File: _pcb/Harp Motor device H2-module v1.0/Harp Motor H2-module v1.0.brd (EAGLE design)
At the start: 58 x 52.5 mm, 80 parts, among them IC1 FT232RL, IC10 OPA365, IC11 74LVC1G125DBV, IC12 74LVC1G125DBV, IC3 LP5907MFX-3.3, IC7 USBLC6-2SC6, IC8 ATXMEGA32A4U, IC9 TLV70033DDCR, T1 DMG1012UW??, T2 DMG1012UW??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

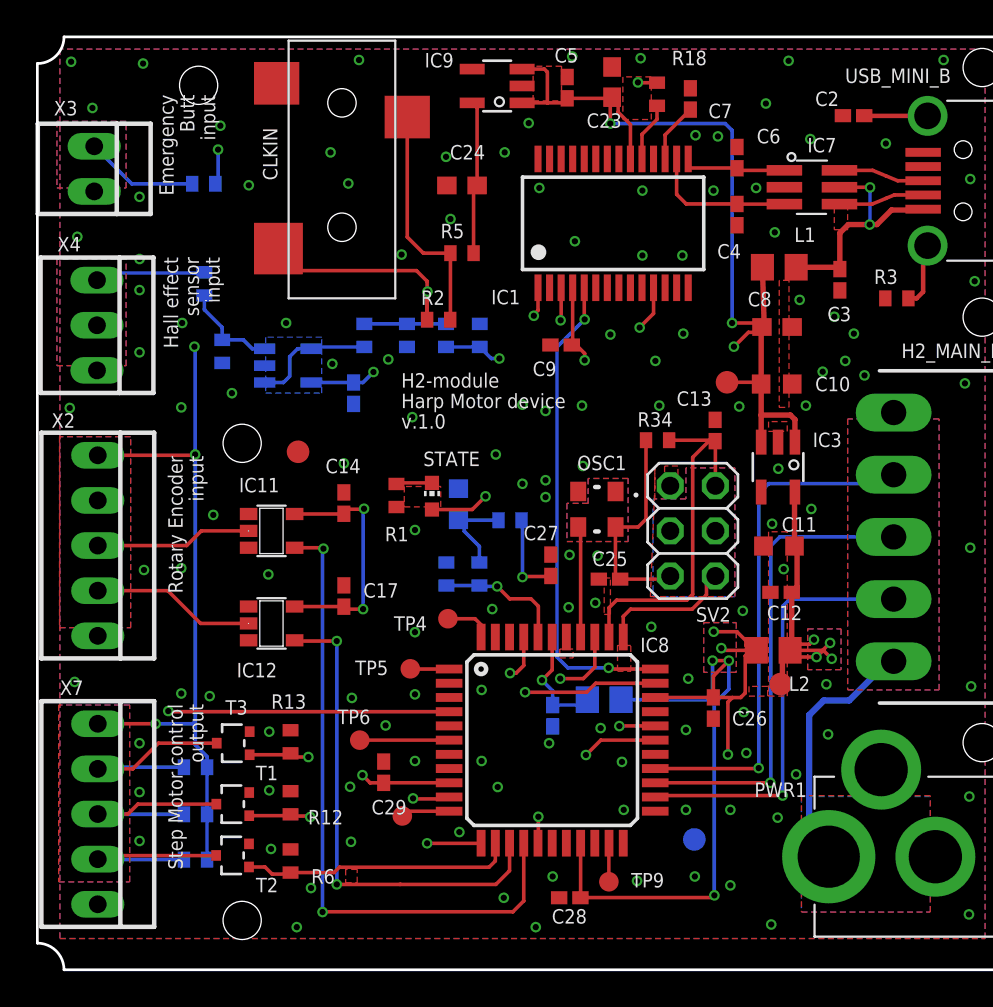
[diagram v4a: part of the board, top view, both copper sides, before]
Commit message: Harp Motor device H2-module v1.0 - last revision with Filipe
- extra R0 on some stages
- IO headers - GND pin was on wrong end
- rebuild user-friend labelling

- still missing OEPS components code & BOM
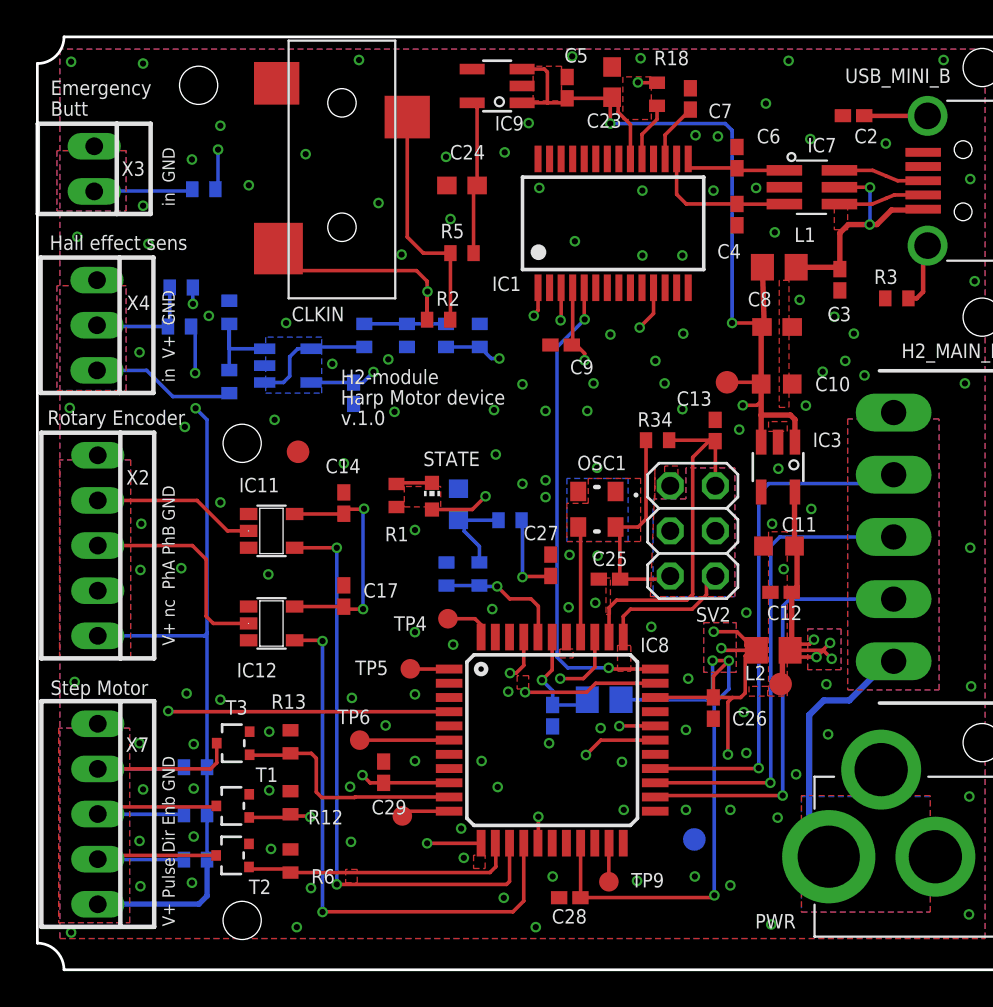
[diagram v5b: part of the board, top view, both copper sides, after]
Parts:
- added R10: DNI, Harp Motor H2-module v1.0:R0402$1
- added R11: 0R, Harp Motor H2-module v1.0:R0402$1
- moved R20 5.68 mm to (10.8, 33.1), turned to 270 degrees
- moved R21 2.24 mm to (10.8, 37.0), turned to 270 degrees
- moved R8 0.30 mm to (9.37, 43.9)
- moved T1 0.10 mm to (11.0, 9.22)
- renumbered PWR1 to PWR
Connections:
- new net N$51: R10.1, R11.1, X4.2
- net +3V3: now also R11.2; no longer X4.2
- net +5V: now also R10.2, X2.5, X7.5; no longer X2.1, X7.1
- net EMERGENCY_INPUT: now also X3.2; no longer X3.1
- net ENCODER_A_PHASE: now also IC12.2; no longer IC11.2
- net ENCODER_B_PHASE: now also IC11.2, X2.2; no longer IC12.2, X2.4
- net GND: now also X2.1, X3.1, X4.1, X7.1; no longer X2.5, X3.2, X4.3, X7.5
- net HALL_EFFCT_IN: now also X4.3; no longer X4.1
- net STEP_ENABLE: now also R14.1, T3.3, X7.2; no longer R16.1, T2.3, X7.4
- net STEP_PULSE: now also R16.1, T2.3, X7.4; no longer R14.1, T3.3, X7.2
- net U_ENCODER_A_PHASE: now also IC12.4; no longer IC11.4
- net U_ENCODER_B_PHASE: now also IC11.4; no longer IC12.4
- net U_STEP_ENABLE: now also IC8.10, R13.2, T3.1; no longer IC8.13, R6.2, T2.1
- net U_STEP_PULSE: now also IC8.13, R6.2, T2.1; no longer IC8.10, R13.2, T3.1
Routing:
- net N$51: track 0.00 -> 6.27 mm
- net U_ENCODER_B_PHASE: track 27.7 -> 33.3 mm
- net +5V: track 121.3 -> 126.7 mm, vias 6 -> 5
- net U_ENCODER_A_PHASE: track 36.9 -> 31.7 mm
- net +3V3: track 224.7 -> 219.8 mm, vias 14 -> 15
- net EMERGENCY_INPUT: track 57.9 -> 54.2 mm
- net ENCODER_A_PHASE: track 8.83 -> 12.2 mm
- net U_STEP_PULSE: track 13.2 -> 15.5 mm, vias 2 -> 0
- net U_STEP_ENABLE: track 15.4 -> 13.4 mm
- net HALL_EFFCT_IN: track 6.23 -> 8.14 mm
- net STEP_ENABLE: track 11.6 -> 12.8 mm
- added copper zone on layer 1, net N$59
- added copper zone on layer 1, net N$60
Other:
- board text added: "Emergency Butt"
- board text added: "Hall effect sens"
- board text added: "Rotary Encoder"
- board text added: "Step Motor"
- board text added: "V+ Pulse Dir Enb GND"
- board text added: "V+ nc PhA PhB GND"
- board text added: "in GND"
- board text added: "in V+ GND"
- board text removed: "Emergency Butt input"
- board text removed: "Hall effect sensor input"
- board text removed: "Rotary Encoder input"
- board text removed: "Step Motor control output"
